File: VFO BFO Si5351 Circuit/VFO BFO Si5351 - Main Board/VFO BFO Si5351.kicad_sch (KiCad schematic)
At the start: 33 parts, among them J1 I2C Bus, J10 VIN +12,8V, J11 GND +5V +9V +12, J12 VFO_Front_Pannel, J2 Band, J3 Mode, J4 AGC, J5 ATT, J6 BFO, J7 TX, J8 IN RTTY, J9 IN S_meter, M1 Si5351A module, U1 ESP32-DEVKITC-32D, U2 PCF8574AP, U3 LM7809, U4 LM7805, U5 24LC32

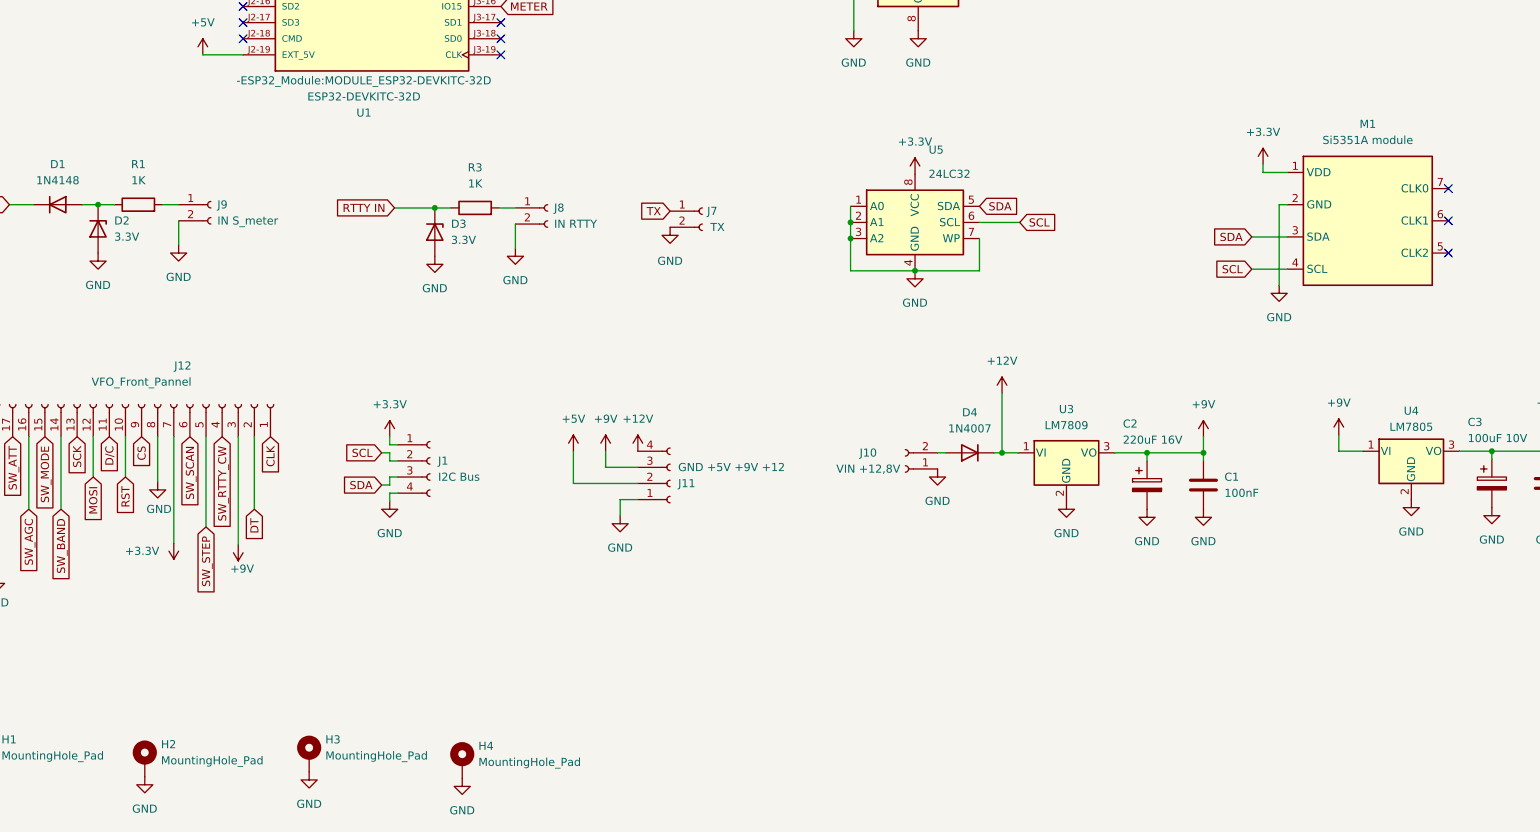
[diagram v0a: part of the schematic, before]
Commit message: PDF distenta componenti e  schemi elettrico e di montaggio
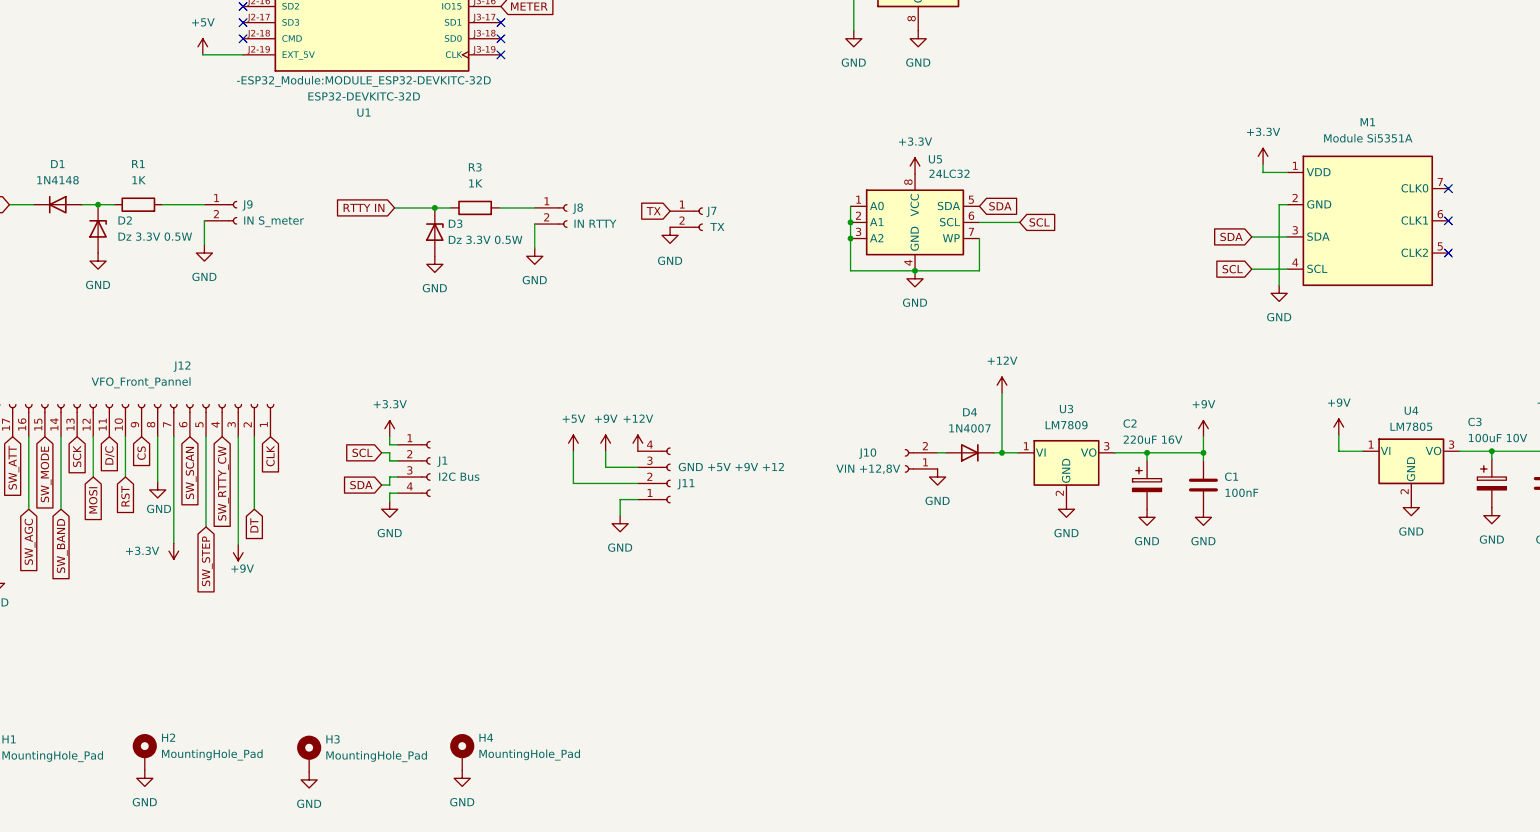
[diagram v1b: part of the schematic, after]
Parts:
- D2, D3: value 3.3V -> Dz 3.3V 0.5W
- M1: value Si5351A module -> Module Si5351A
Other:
- moved on the sheet: H2, H4, J8, J9
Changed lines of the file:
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@@
 	(wire
 		(pts
-			(xy 110.998 101.092) (xy 110.998 104.902)
+			(xy 114.046 101.092) (xy 114.046 104.902)
 		)
 		(stroke
@@
 	(wire
 		(pts
-			(xy 57.912 100.584) (xy 57.912 104.394)
+			(xy 61.976 100.584) (xy 61.976 104.394)
 		)
 		(stroke
@@
 	(wire
 		(pts
-			(xy 55.372 98.044) (xy 57.912 98.044)
+			(xy 55.372 98.044) (xy 61.976 98.044)
 		)
 		(stroke
@@
 	(wire
 		(pts
-			(xy 108.458 98.552) (xy 110.998 98.552)
+			(xy 108.458 98.552) (xy 114.046 98.552)
 		)
 		(stroke
@@
 		(dnp no)
 		(property "Reference" "U5"
-			(at 176.1333 89.408 0)
+			(at 176.022 90.932 0)
 			(effects
 				(font
@@
 	(symbol
 		(lib_id "power:GND")
-		(at 57.912 104.394 0)
+		(at 61.976 104.394 0)
 		(unit 1)
 		(exclude_from_sim no)
@@
 		(fields_autoplaced yes)
 		(property "Reference" "#PWR013"
-			(at 57.912 110.744 0)
+			(at 61.976 110.744 0)
 			(effects
 				(font
@@
 		)
 		(property "Value" "GND"
-			(at 57.912 109.474 0)
+			(at 61.976 109.474 0)
 			(effects
 				(font
@@
 		)
 		(property "Footprint" ""
-			(at 57.912 104.394 0)
+			(at 61.976 104.394 0)
 			(effects
 				(font
@@
 		)
 		(property "Datasheet" ""
-			(at 57.912 104.394 0)
+			(at 61.976 104.394 0)
 			(effects
 				(font
@@
 		)
 		(property "Description" "Power symbol creates a global label with name \"GND\" , ground"
-			(at 57.912 104.394 0)
+			(at 61.976 104.394 0)
 			(effects
 				(font
@@
 	(symbol
 		(lib_id "power:GND")
-		(at 110.998 104.902 0)
+		(at 114.046 104.902 0)
 		(unit 1)
 		(exclude_from_sim no)
@@
 		(fields_autoplaced yes)
 		(property "Reference" "#PWR024"
-			(at 110.998 111.252 0)
+			(at 114.046 111.252 0)
 			(effects
 				(font
@@
 		)
 		(property "Value" "GND"
-			(at 110.998 109.982 0)
+			(at 114.046 109.982 0)
 			(effects
 				(font
@@
 		)
 		(property "Footprint" ""
-			(at 110.998 104.902 0)
+			(at 114.046 104.902 0)
 			(effects
 				(font
@@
 		)
 		(property "Datasheet" ""
-			(at 110.998 104.902 0)
+			(at 114.046 104.902 0)
 			(effects
 				(font
@@
 		)
 		(property "Description" "Power symbol creates a global label with name \"GND\" , ground"
-			(at 110.998 104.902 0)
+			(at 114.046 104.902 0)
 			(effects
 				(font
@@
 	(symbol
 		(lib_id "Connector:Conn_01x02_Socket")
-		(at 116.078 98.552 0)
+		(at 119.126 98.552 0)
 		(unit 1)
 		(exclude_from_sim no)
@@
 		(fields_autoplaced yes)
 		(property "Reference" "J8"
-			(at 117.094 98.5519 0)
+			(at 120.142 98.5519 0)
 			(effects
 				(font
@@
 		)
 		(property "Value" "IN RTTY"
-			(at 117.094 101.0919 0)
+			(at 120.142 101.0919 0)
 			(effects
 				(font
@@
 		)
 		(property "Footprint" "Connector_JST:JST_EH_B2B-EH-A_1x02_P2.50mm_Vertical"
-			(at 116.078 98.552 0)
+			(at 119.126 98.552 0)
 			(effects
 				(font
@@
 		)
 		(property "Datasheet" "~"
-			(at 116.078 98.552 0)
+			(at 119.126 98.552 0)
 			(effects
 				(font
@@
 		)
 		(property "Description" "Generic connector, single row, 01x02, script generated"
-			(at 116.078 98.552 0)
+			(at 119.126 98.552 0)
 			(effects
 				(font
@@
 	(symbol
 		(lib_id "power:GND")
-		(at 52.578 188.214 0)
+		(at 52.578 187.198 0)
 		(unit 1)
 		(exclude_from_sim no)
@@
 		(fields_autoplaced yes)
 		(property "Reference" "#PWR016"
-			(at 52.578 194.564 0)
+			(at 52.578 193.548 0)
 			(effects
 				(font
@@
 		)
 		(property "Value" "GND"
-			(at 52.578 193.294 0)
+			(at 52.578 192.278 0)
 			(effects
 				(font
@@
 		)
 		(property "Footprint" ""
-			(at 52.578 188.214 0)
+			(at 52.578 187.198 0)
 			(effects
 				(font
@@
 		)
 		(property "Datasheet" ""
-			(at 52.578 188.214 0)
+			(at 52.578 187.198 0)
 			(effects
 				(font
@@
 		)
 		(property "Description" "Power symbol creates a global label with name \"GND\" , ground"
-			(at 52.578 188.214 0)
+			(at 52.578 187.198 0)
 			(effects
 				(font
@@
 	(symbol
 		(lib_id "power:GND")
-		(at 102.616 188.468 0)
+		(at 102.616 187.198 0)
 		(unit 1)
 		(exclude_from_sim no)
@@
 		(fields_autoplaced yes)
 		(property "Reference" "#PWR023"
-			(at 102.616 194.818 0)
+			(at 102.616 193.548 0)
 			(effects
 				(font
@@
 		)
 		(property "Value" "GND"
-			(at 102.616 193.548 0)
+			(at 102.616 192.278 0)
 			(effects
 				(font
@@
 		)
 		(property "Footprint" ""
-			(at 102.616 188.468 0)
+			(at 102.616 187.198 0)
 			(effects
 				(font
@@
 		)
 		(property "Datasheet" ""
-			(at 102.616 188.468 0)
+			(at 102.616 187.198 0)
 			(effects
 				(font
@@
 		)
 		(property "Description" "Power symbol creates a global label with name \"GND\" , ground"
-			(at 102.616 188.468 0)
+			(at 102.616 187.198 0)
 			(effects
 				(font
@@
 		(on_board yes)
 		(dnp no)
-		(fields_autoplaced yes)
 		(property "Reference" "D2"
-			(at 47.752 100.5839 90)
+			(at 48.26 100.5839 90)
 			(effects
 				(font
@@
 			)
 		)
-		(property "Value" "3.3V"
-			(at 47.752 103.1239 90)
+		(property "Value" "Dz 3.3V 0.5W"
+			(at 48.26 103.1239 90)
 			(effects
 				(font
@@
 	(symbol
 		(lib_id "Mechanical:MountingHole_Pad")
-		(at 52.578 185.674 0)
+		(at 52.578 184.658 0)
 		(unit 1)
 		(exclude_from_sim yes)
@@
 		(fields_autoplaced yes)
 		(property "Reference" "H2"
-			(at 55.118 183.1339 0)
+			(at 55.118 182.1179 0)
 			(effects
 				(font
@@
 		)
 		(property "Value" "MountingHole_Pad"
-			(at 55.118 185.6739 0)
+			(at 55.118 184.6579 0)
 			(effects
 				(font
@@
 		)
 		(property "Footprint" "MountingHole:MountingHole_3.2mm_M3_DIN965_Pad_TopBottom"
-			(at 52.578 185.674 0)
+			(at 52.578 184.658 0)
 			(effects
 				(font
@@
 		)
 		(property "Datasheet" "~"
-			(at 52.578 185.674 0)
+			(at 52.578 184.658 0)
 			(effects
 				(font
@@
 		)
 		(property "Description" "Mounting Hole with connection"
-			(at 52.578 185.674 0)
+			(at 52.578 184.658 0)
 			(effects
 				(font
@@
 		(fields_autoplaced yes)
 		(property "Reference" "M1"
-			(at 245.364 85.344 0)
+			(at 245.364 85.09 0)
 			(effects
 				(font
@@
 			)
 		)
-		(property "Value" "Si5351A module"
-			(at 245.364 87.884 0)
+		(property "Value" "Module Si5351A"
+			(at 245.364 87.63 0)
 			(effects
 				(font
@@
 		(fields_autoplaced yes)
 		(property "Reference" "D3"
-			(at 100.838 101.0919 90)
+			(at 100.33 101.0919 90)
 			(effects
 				(font
@@
 			)
 		)
-		(property "Value" "3.3V"
-			(at 100.838 103.6319 90)
+		(property "Value" "Dz 3.3V 0.5W"
+			(at 100.33 103.6319 90)
 			(effects
 				(font
@@
 	(symbol
 		(lib_id "Mechanical:MountingHole_Pad")
-		(at 102.616 185.928 0)
+		(at 102.616 184.658 0)
 		(unit 1)
 		(exclude_from_sim yes)
@@
 		(fields_autoplaced yes)
 		(property "Reference" "H4"
-			(at 105.156 183.3879 0)
+			(at 105.156 182.1179 0)
 			(effects
 				(font
@@
 		)
 		(property "Value" "MountingHole_Pad"
-			(at 105.156 185.9279 0)
+			(at 105.156 184.6579 0)
 			(effects
 				(font
@@
 		)
 		(property "Footprint" "MountingHole:MountingHole_3.2mm_M3_DIN965_Pad_TopBottom"
-			(at 102.616 185.928 0)
+			(at 102.616 184.658 0)
 			(effects
 				(font
@@
 		)
 		(property "Datasheet" "~"
-			(at 102.616 185.928 0)
+			(at 102.616 184.658 0)
 			(effects
 				(font
@@
 		)
 		(property "Description" "Mounting Hole with connection"
-			(at 102.616 185.928 0)
+			(at 102.616 184.658 0)
 			(effects
 				(font
@@
 	(symbol
 		(lib_id "Connector:Conn_01x02_Socket")
-		(at 62.992 98.044 0)
+		(at 67.056 98.044 0)
 		(unit 1)
 		(exclude_from_sim no)
@@
 		(fields_autoplaced yes)
 		(property "Reference" "J9"
-			(at 64.008 98.0439 0)
+			(at 68.072 98.0439 0)
 			(effects
 				(font
@@
 		)
 		(property "Value" "IN S_meter"
-			(at 64.008 100.5839 0)
+			(at 68.072 100.5839 0)
 			(effects
 				(font
@@
 		)
 		(property "Footprint" "Connector_JST:JST_EH_B2B-EH-A_1x02_P2.50mm_Vertical"
-			(at 62.992 98.044 0)
+			(at 67.056 98.044 0)
 			(effects
 				(font
@@
 		)
 		(property "Datasheet" "~"
-			(at 62.992 98.044 0)
+			(at 67.056 98.044 0)
 			(effects
 				(font
@@
 		)
 		(property "Description" "Generic connector, single row, 01x02, script generated"
-			(at 62.992 98.044 0)
+			(at 67.056 98.044 0)
 			(effects
 				(font
